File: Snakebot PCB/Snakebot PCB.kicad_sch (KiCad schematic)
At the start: 15 parts, among them J1 Conn_01x02_Pin, U1 RP2040, U2 W25Q128JVSIQ, U3 AMS1117-3.3, X1 ABM8-272-T3

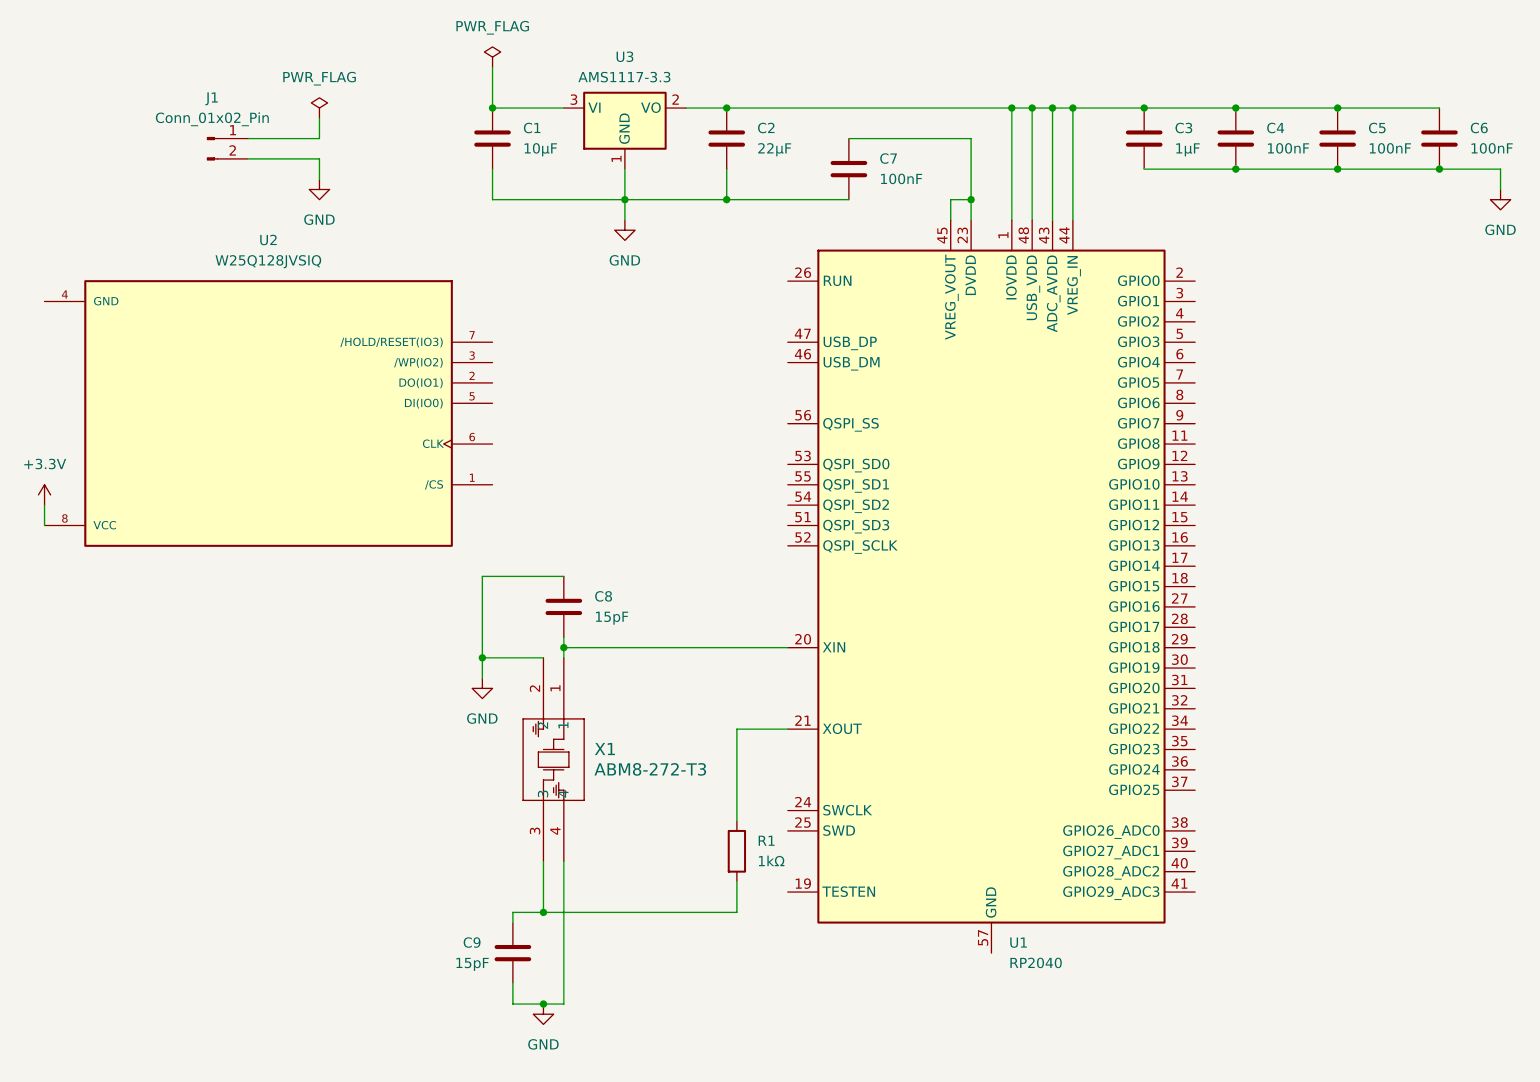
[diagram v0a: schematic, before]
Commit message: Add files via upload
minor changes to schematic including establishing connections between rp2040 and memory. Also added ground and voltage in other places
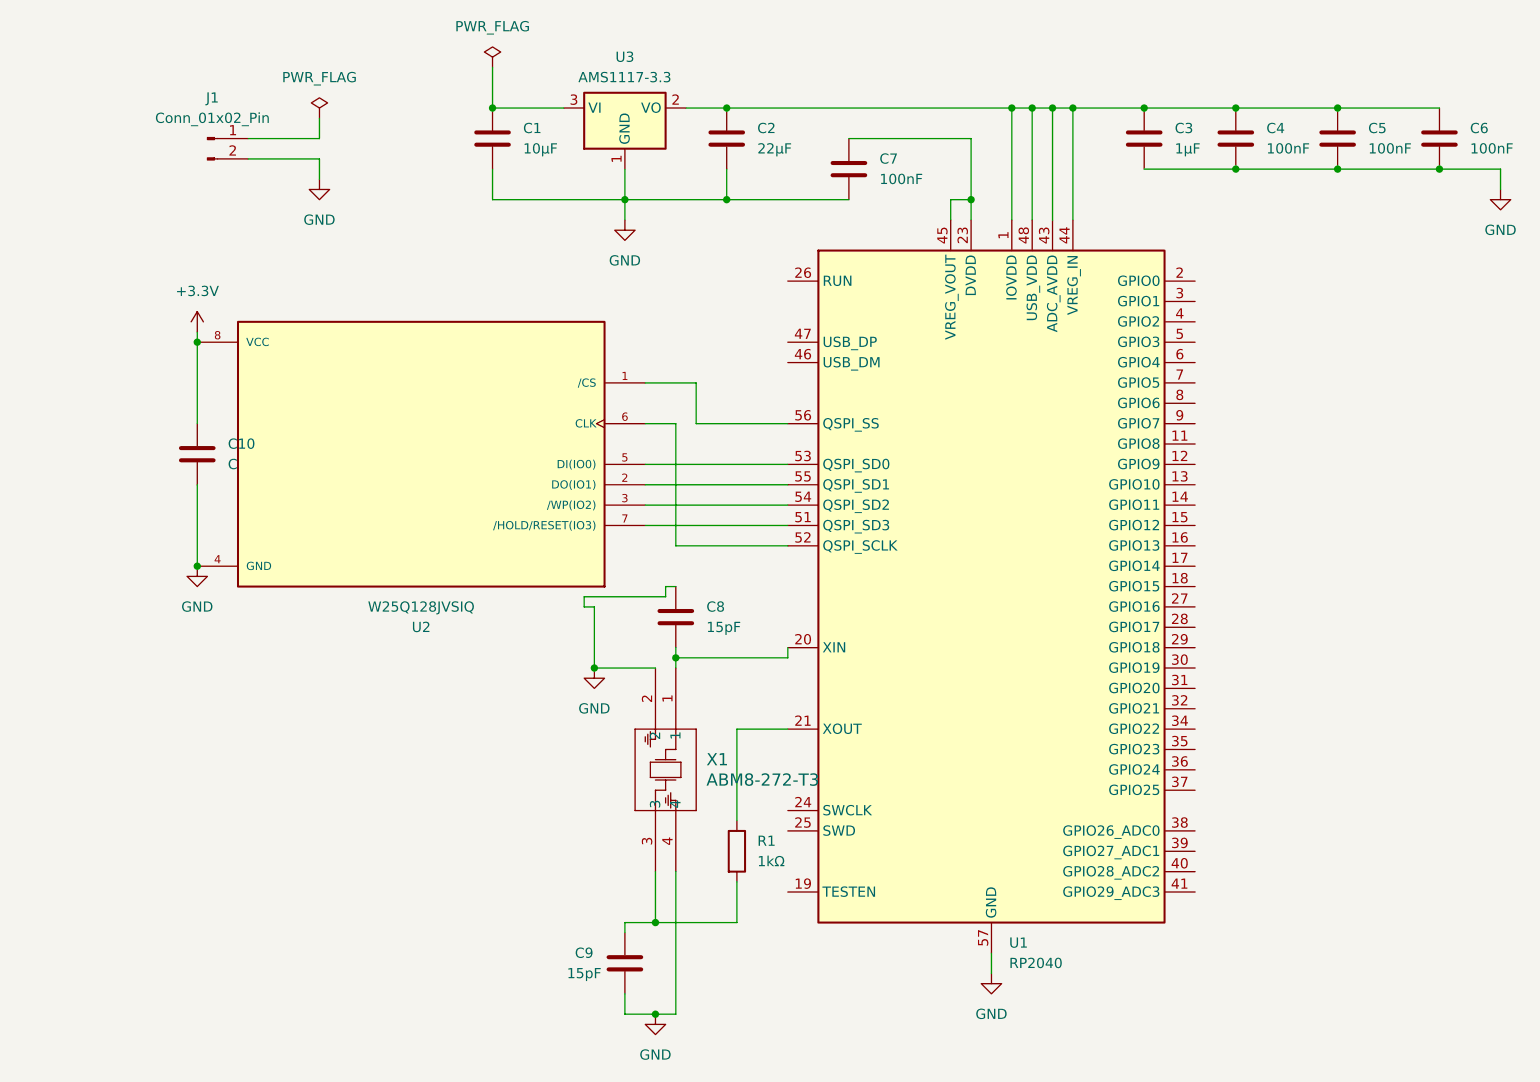
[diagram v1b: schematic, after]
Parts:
- added C10: C, symbol Device:C
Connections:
- net +3.3V: now also C10.1
- net GND: now also U1.57 (GND), U2.4 (GND), C10.2
- net at U2.1 (/CS): now also U1.56 (QSPI_SS)
- net at U2.2 (DO(IO1)): now also U1.55 (QSPI_SD1)
- net at U2.3 (/WP(IO2)): now also U1.54 (QSPI_SD2)
- net at U2.5 (DI(IO0)): now also U1.53 (QSPI_SD0)
- net at U2.6 (CLK): now also U1.52 (QSPI_SCLK)
- net at U2.7 (/HOLD/RESET(IO3)): now also U1.51 (QSPI_SD3)
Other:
- moved on the sheet: C8, C9, U2, X1
